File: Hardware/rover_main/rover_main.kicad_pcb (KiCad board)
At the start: 2 copper layers, 85 x 70 mm, 38 parts, among them J1 BATT, J10 Analog, J2 BME280, J3 CSS811, J4 DRIVERS, J5 GY-87, J7 FTDI, J8 Digital, U1 LD1117A33, U2 MCP732831CHARGER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

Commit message: move edge cuts ESP32
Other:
- outline, holes or cut-outs redrawn
- board text added: "I2C BAST"
- board text removed: "I2C BATS"
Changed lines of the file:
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@@
     (43 Eco2.User user)
     (44 Edge.Cuts user)
-    (45 Margin user)
+    (45 Margin user hide)
     (46 B.CrtYd user)
     (47 F.CrtYd user)
@@
   (gr_line (start 112 98) (end 114 98) (layer Dwgs.User) (width 0.15))
   (gr_line (start 112 82) (end 112 98) (layer Dwgs.User) (width 0.15))
-  (gr_arc (start 102.5 105.9) (end 102.5 103.4) (angle -90) (layer Edge.Cuts) (width 0.05))
+  (gr_arc (start 102.5 105.8) (end 102.5 103.3) (angle -90) (layer Edge.Cuts) (width 0.05))
   (dimension 2.5 (width 0.15) (layer Margin)
     (gr_text "2.500 mm" (at 106.1 104.65 270) (layer Margin)
@@
     (effects (font (size 1 1) (thickness 0.15)))
   )
-  (gr_text "I2C BATS" (at 153.416 106.934) (layer B.SilkS)
+  (gr_text "I2C BAST" (at 153.416 106.934) (layer B.SilkS)
     (effects (font (size 1 1) (thickness 0.15)) (justify mirror))
   )
@@
     (arrow2b (pts (xy 82.5 60.1) (xy 83.086421 61.226504)))
   )
-  (gr_line (start 114.45 103.4) (end 102.5 103.4) (layer Edge.Cuts) (width 0.05))
-  (gr_line (start 114.45 76.4) (end 114.45 103.4) (layer Edge.Cuts) (width 0.05))
+  (gr_line (start 114.45 103.3) (end 102.5 103.3) (layer Edge.Cuts) (width 0.05))
+  (gr_line (start 114.45 76.4) (end 114.45 103.3) (layer Edge.Cuts) (width 0.05))
   (gr_line (start 102.5 76.4) (end 114.45 76.4) (layer Edge.Cuts) (width 0.05))
   (gr_line (start 100 73.9) (end 100 65.1) (layer Edge.Cuts) (width 0.05))
@@
   (gr_line (start 141.181 112.312) (end 141.181 127.254) (layer F.SilkS) (width 0.12))
   (gr_line (start 105 60.1) (end 180 60.1) (layer Edge.Cuts) (width 0.05))
-  (gr_line (start 100 125.05) (end 100 105.9) (layer Edge.Cuts) (width 0.05))
+  (gr_line (start 100 125.05) (end 100 105.8) (layer Edge.Cuts) (width 0.05))
   (gr_line (start 180 130.1) (end 105 130.1) (layer Edge.Cuts) (width 0.05))
   (gr_line (start 185 65.1) (end 185 125.1) (layer Edge.Cuts) (width 0.05))

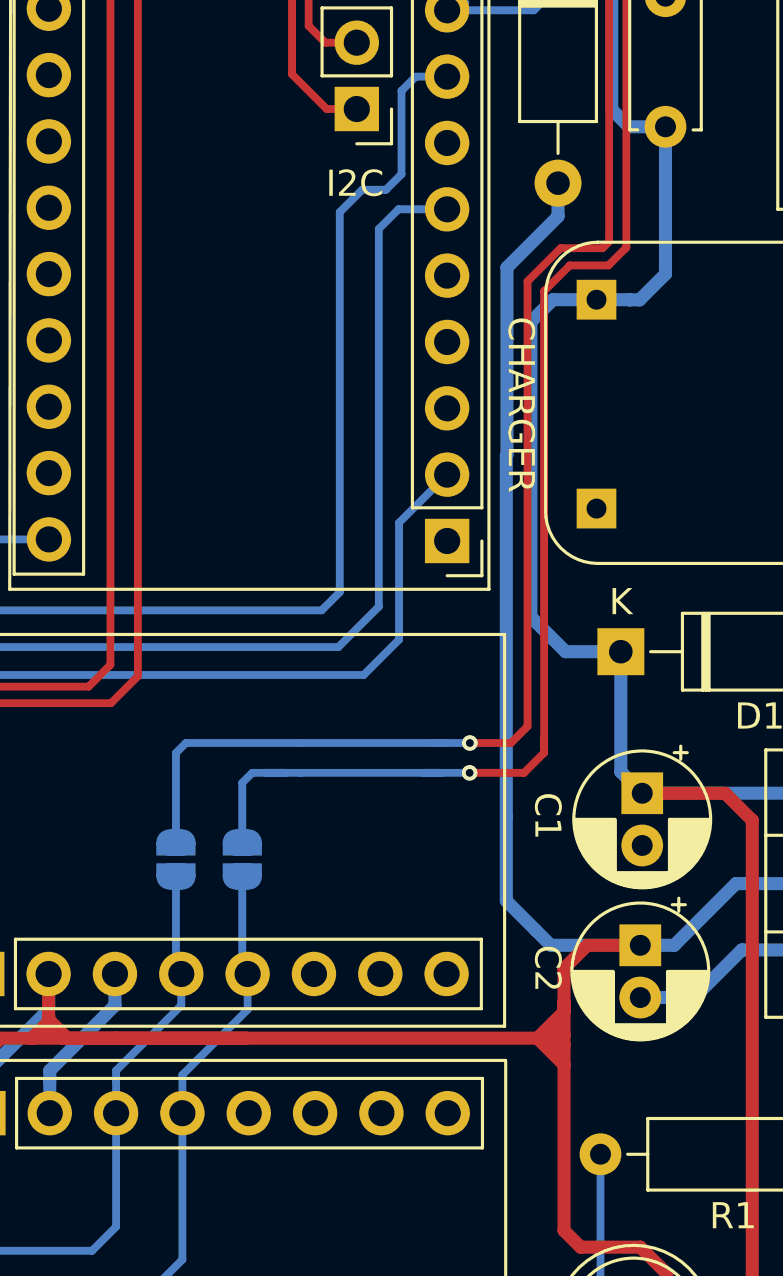
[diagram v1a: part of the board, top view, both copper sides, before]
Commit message: rerouting CCS811
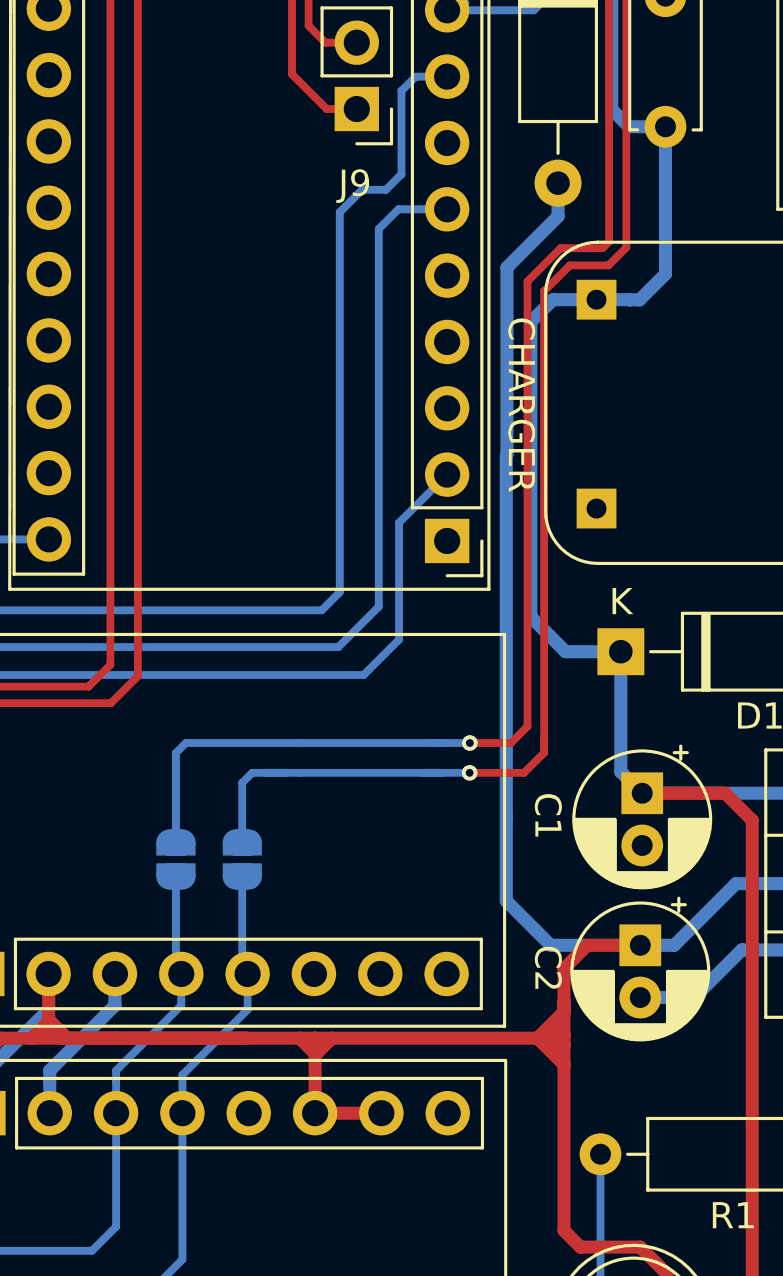
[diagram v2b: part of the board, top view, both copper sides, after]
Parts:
- renumbered SDA to J6, I2C to J9
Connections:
- J3 pad 5: /WAKE -> GND
- J3 pad 6: /INTCSS -> +3V3
- J3 pad 7: /RESET -> +3V3
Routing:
- net +3V3: track 170.8 -> 177.9 mm
